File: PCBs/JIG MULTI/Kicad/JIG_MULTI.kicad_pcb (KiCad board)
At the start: 2 copper layers, 85.1 x 73.7 mm, 19 parts, among them U0 12pad, U1 12pad

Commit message: Fixed resistor value for 5V circuit
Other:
- board text added: "R1 = 2K R2 = 1K R3 = 1K R4 = 150 R5 = 2K R6 = 7.5K"
- board text removed: "R1 = 1K R2 = 1K R3 = 1K R4 = 150 R5 = 2K R6 = 7.5K"
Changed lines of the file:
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@@
     (effects (font (size 2 2) (thickness 0.4) bold) (justify left bottom))
   )
-  (gr_text "R1 = 1K\nR2 = 1K\nR3 = 1K\nR4 = 150\nR5 = 2K\nR6 = 7.5K" (at 43.18 96.52) (layer "F.SilkS")
+  (gr_text "R1 = 2K\nR2 = 1K\nR3 = 1K\nR4 = 150\nR5 = 2K\nR6 = 7.5K" (at 43.18 96.52) (layer "F.SilkS")
     (effects (font (size 2 2) (thickness 0.1)) (justify left bottom))
   )

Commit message: Added a warning label at the back of the board
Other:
- board text added: "** CAUTION ** Some UART modules advertised as 5V or with a jumper to 5V do NOT shift the power levels for UART TX/RX which will operate at 3.3V, Please measure voltage on your UART module between TX and GND. if it runs at 3.3V Replace R5 to a 1K ohms resistor."
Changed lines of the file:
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@@
   (gr_line (start 58.42 93.98) (end 58.42 99.06)
     (stroke (width 0.25) (type default)) (layer "F.Cu"))
+  (gr_rect (start 33.5 43.18) (end 114.78 55.88)
+    (stroke (width 0.2) (type default)) (fill none) (layer "B.SilkS"))
   (gr_rect (start 106.68 91.02) (end 111.76 96.52)
     (stroke (width 0.2) (type default)) (fill none) (layer "F.SilkS"))
@@
     (effects (font (size 2 2) (thickness 0.4) bold) (justify left bottom mirror))
   )
+  (gr_text "** CAUTION ** \n\n\nSome UART modules advertised as 5V or with a jumper to 5V do NOT shift the power levels for UART TX/RX \nwhich will operate at 3.3V, Please measure voltage on your UART module between TX and GND.\nif it runs at 3.3V Replace R5 to a 1K ohms resistor." (at 114.3 53.34) (layer "B.SilkS")
+    (effects (font (size 1 1) (thickness 0.2) bold) (justify left bottom mirror))
+  )
   (gr_text "PCH-1K Only" (at 105 80.5 90) (layer "F.SilkS")

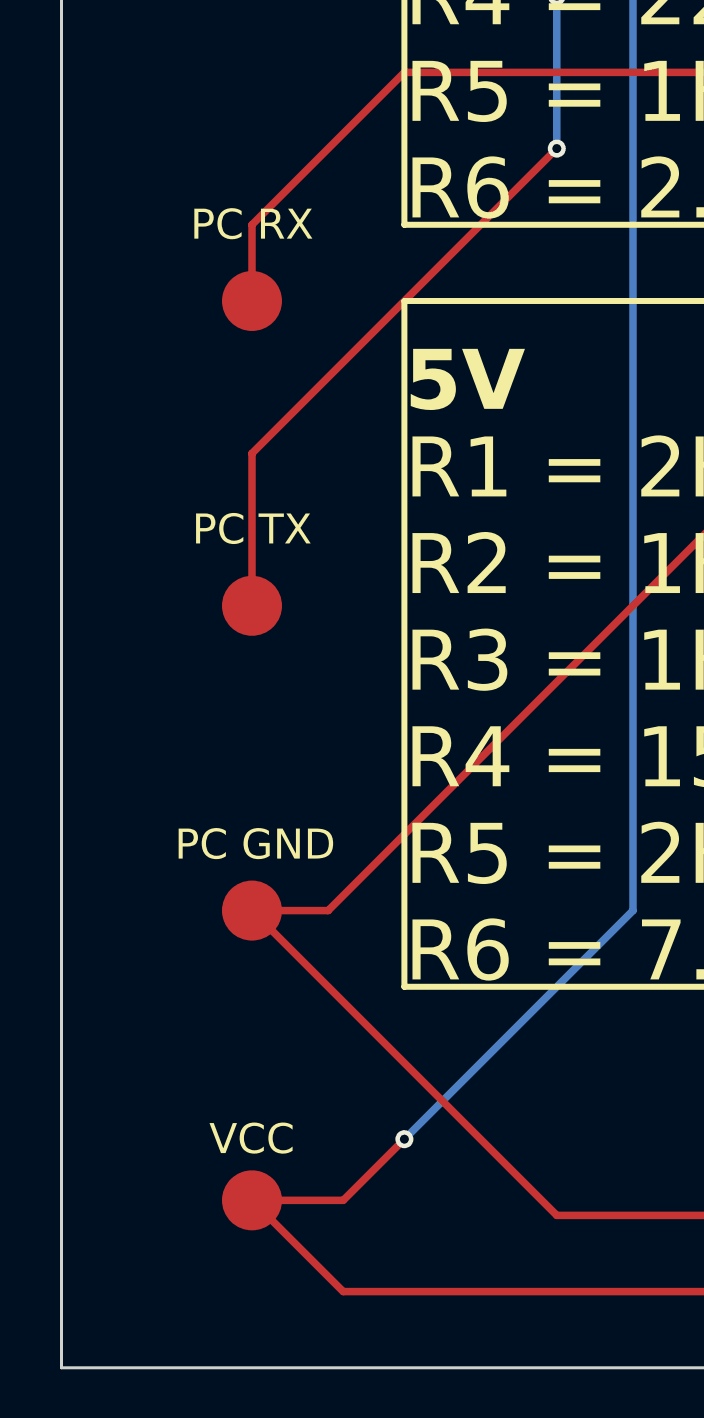
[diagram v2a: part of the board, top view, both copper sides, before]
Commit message: Used proper footprints for some of the pads that were missing them.
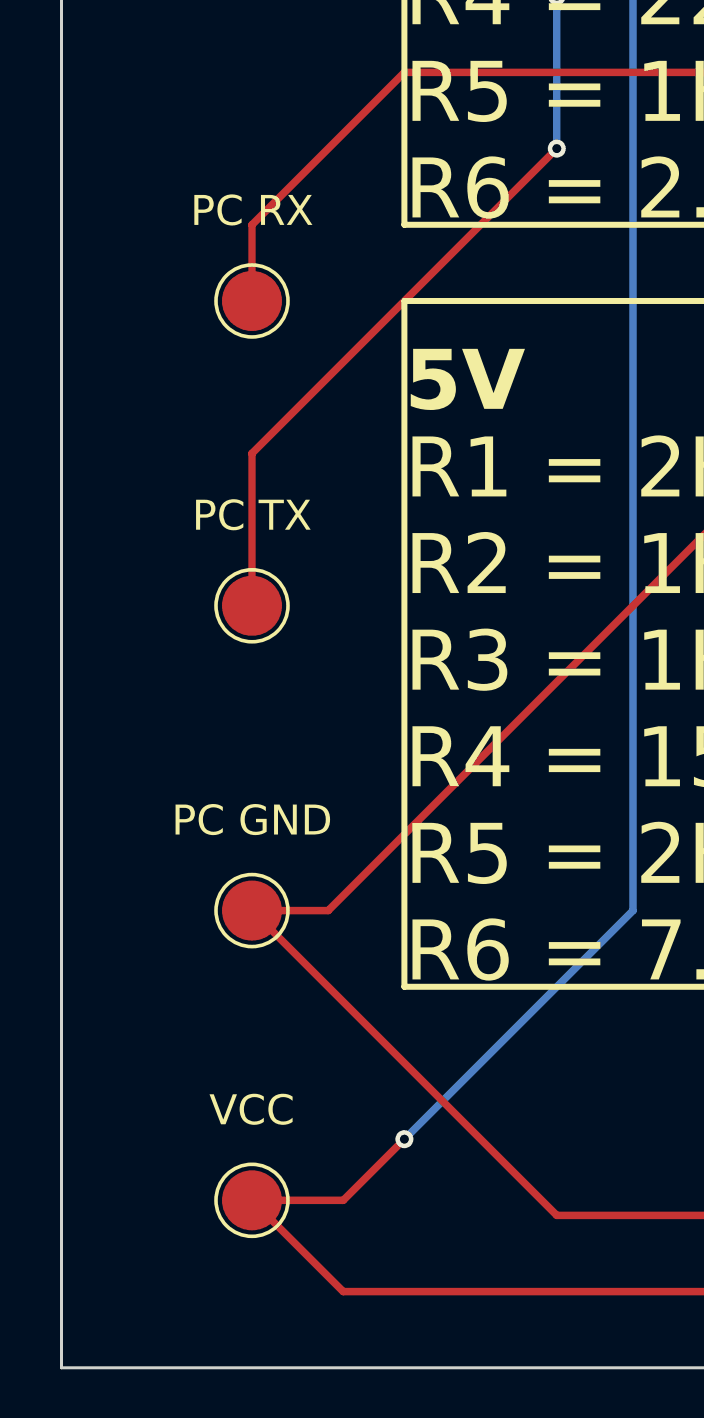
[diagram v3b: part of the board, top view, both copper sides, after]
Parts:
- removed ? (x4): , 
- added PC GND: TestPoint_Pad_D2.0mm, TestPoint:TestPoint_Pad_D2.0mm, F.Cu at (38.1, 94.0)
- added PC RX: TestPoint_Pad_D2.0mm, TestPoint:TestPoint_Pad_D2.0mm, F.Cu at (38.1, 73.7)
- added PC TX: TestPoint_Pad_D2.0mm, TestPoint:TestPoint_Pad_D2.0mm, F.Cu at (38.1, 83.8)
- added VCC: TestPoint_Pad_D2.0mm, TestPoint:TestPoint_Pad_D2.0mm, F.Cu at (38.1, 103.6)
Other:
- board text removed: "PC GND"
- board text removed: "PC RX"
- board text removed: "PC TX"
- board text removed: "VCC"
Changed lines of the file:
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@@
     (pad "12" thru_hole circle (at 27.94 0) (size 1.524 1.524) (drill 0.914) (layers "*.Cu" "*.Paste" "*.Mask"))
+  )
+  (footprint "TestPoint:TestPoint_Pad_D2.0mm" (layer "F.Cu")
+    (at 38.1 83.82)
+    (descr "SMD pad as test Point, diameter 2.0mm")
+    (tags "test point SMD pad")
+    (attr exclude_from_pos_files exclude_from_bom)
+    (fp_text reference "PC TX" (at 0 -2.998) (layer "F.SilkS")
+        (effects (font (size 1 1) (thickness 0.15)))
+    )
+    (fp_text value "TestPoint_Pad_D2.0mm" (at 0 2.05) (layer "F.Fab")
+        (effects (font (size 1 1) (thickness 0.15)))
+    )
+    (fp_text user "${REFERENCE}" (at 0 -2) (layer "F.Fab")
+        (effects (font (size 1 1) (thickness 0.15)))
+    )
+    (fp_circle (center 0 0) (end 0 1.2)
+      (stroke (width 0.12) (type solid)) (fill none) (layer "F.SilkS"))
+    (fp_circle (center 0 0) (end 1.5 0)
+      (stroke (width 0.05) (type solid)) (fill none) (layer "F.CrtYd"))
+    (pad "2" smd circle (at 0 0) (size 2 2) (layers "F.Cu" "F.Mask"))
   )
   (footprint "Resistor_THT:R_Axial_DIN0309_L9.0mm_D3.2mm_P12.70mm_Horizontal" (layer "F.Cu")
@@
     (pad "8" smd circle (at 0 0) (size 2 2) (layers "F.Cu" "F.Mask"))
   )
-  (footprint "" (layer "F.Cu")
-    (at 38.1 103.637944)
-    (fp_text reference "" (at 0 0) (layer "F.SilkS")
-        (effects (font (size 1.27 1.27) (thickness 0.15)))
-    )
-    (fp_text value "" (at 0 0) (layer "F.SilkS")
-        (effects (font (size 1.27 1.27) (thickness 0.15)))
-    )
-    (pad "4" smd circle (at 0 0) (size 2 2) (layers "F.Cu" "F.Mask"))
-  )
   (footprint "Resistor_THT:R_Axial_DIN0309_L9.0mm_D3.2mm_P12.70mm_Horizontal" (layer "F.Cu")
     (at 58.42 99.06)
@@
       (stroke (width 0.05) (type solid)) (fill none) (layer "F.CrtYd"))
     (pad "6" smd circle (at 0 0) (size 2 2) (layers "F.Cu" "F.Mask"))
+  )
+  (footprint "TestPoint:TestPoint_Pad_D2.0mm" (layer "F.Cu")
+    (at 38.1 103.637944)
+    (descr "SMD pad as test Point, diameter 2.0mm")
+    (tags "test point SMD pad")
+    (attr exclude_from_pos_files exclude_from_bom)
+    (fp_text reference "VCC" (at 0 -2.998) (layer "F.SilkS")
+        (effects (font (size 1 1) (thickness 0.15)))
+    )
+    (fp_text value "TestPoint_Pad_D2.0mm" (at 0 2.05) (layer "F.Fab")
+        (effects (font (size 1 1) (thickness 0.15)))
+    )
+    (fp_text user "${REFERENCE}" (at 0 -2) (layer "F.Fab")
+        (effects (font (size 1 1) (thickness 0.15)))
+    )
+    (fp_circle (center 0 0) (end 0 1.2)
+      (stroke (width 0.12) (type solid)) (fill none) (layer "F.SilkS"))
+    (fp_circle (center 0 0) (end 1.5 0)
+      (stroke (width 0.05) (type solid)) (fill none) (layer "F.CrtYd"))
+    (pad "4" smd circle (at 0 0) (size 2 2) (layers "F.Cu" "F.Mask"))
+  )
+  (footprint "TestPoint:TestPoint_Pad_D2.0mm" (layer "F.Cu")
+    (at 38.1 73.66)
+    (descr "SMD pad as test Point, diameter 2.0mm")
+    (tags "test point SMD pad")
+    (attr exclude_from_pos_files exclude_from_bom)
+    (fp_text reference "PC RX" (at 0 -2.998) (layer "F.SilkS")
+        (effects (font (size 1 1) (thickness 0.15)))
+    )
+    (fp_text value "TestPoint_Pad_D2.0mm" (at 0 2.05) (layer "F.Fab")
+        (effects (font (size 1 1) (thickness 0.15)))
+    )
+    (fp_text user "${REFERENCE}" (at 0 -2) (layer "F.Fab")
+        (effects (font (size 1 1) (thickness 0.15)))
+    )
+    (fp_circle (center 0 0) (end 0 1.2)
+      (stroke (width 0.12) (type solid)) (fill none) (layer "F.SilkS"))
+    (fp_circle (center 0 0) (end 1.5 0)
+      (stroke (width 0.05) (type solid)) (fill none) (layer "F.CrtYd"))
+    (pad "1" smd circle (at 0 0) (size 2 2) (layers "F.Cu" "F.Mask"))
   )
   (footprint "Resistor_THT:R_Axial_DIN0309_L9.0mm_D3.2mm_P12.70mm_Horizontal" (layer "F.Cu")
@@
     (pad "29" thru_hole oval (at 11.5 1.5) (size 1 2) (drill oval 0.75 1.75) (layers "*.Cu" "*.Paste" "*.Mask"))
   )
-  (footprint "" (layer "F.Cu")
-    (at 38.1 73.66)
-    (fp_text reference "" (at 0 0) (layer "F.SilkS")
-        (effects (font (size 1.27 1.27) (thickness 0.15)))
-    )
-    (fp_text value "" (at 0 0) (layer "F.SilkS")
-        (effects (font (size 1.27 1.27) (thickness 0.15)))
-    )
-    (pad "1" smd circle (at 0 0) (size 2 2) (layers "F.Cu" "F.Mask"))
-  )
-  (footprint "" (layer "F.Cu")
+  (footprint "TestPoint:TestPoint_Pad_D2.0mm" (layer "F.Cu")
     (at 38.1 93.98)
-    (fp_text reference "" (at 0 0) (layer "F.SilkS")
-        (effects (font (size 1.27 1.27) (thickness 0.15)))
-    )
-    (fp_text value "" (at 0 0) (layer "F.SilkS")
-        (effects (font (size 1.27 1.27) (thickness 0.15)))
-    )
+    (descr "SMD pad as test Point, diameter 2.0mm")
+    (tags "test point SMD pad")
+    (attr exclude_from_pos_files exclude_from_bom)
+    (fp_text reference "PC GND" (at 0 -2.998) (layer "F.SilkS")
+        (effects (font (size 1 1) (thickness 0.15)))
+    )
+    (fp_text value "TestPoint_Pad_D2.0mm" (at 0 2.05) (layer "F.Fab")
+        (effects (font (size 1 1) (thickness 0.15)))
+    )
+    (fp_text user "${REFERENCE}" (at 0 -2) (layer "F.Fab")
+        (effects (font (size 1 1) (thickness 0.15)))
+    )
+    (fp_circle (center 0 0) (end 0 1.2)
+      (stroke (width 0.12) (type solid)) (fill none) (layer "F.SilkS"))
+    (fp_circle (center 0 0) (end 1.5 0)
+      (stroke (width 0.05) (type solid)) (fill none) (layer "F.CrtYd"))
     (pad "3" smd circle (at 0 0) (size 2 2) (layers "F.Cu" "F.Mask"))
   )
@@
       (rotate (xyz 0 0 0))
     )
-  )
-  (footprint "" (layer "F.Cu")
-    (at 38.1 83.82)
-    (fp_text reference "" (at 0 0) (layer "F.SilkS")
-        (effects (font (size 1.27 1.27) (thickness 0.15)))
-    )
-    (fp_text value "" (at 0 0) (layer "F.SilkS")
-        (effects (font (size 1.27 1.27) (thickness 0.15)))
-    )
-    (pad "2" smd circle (at 0 0) (size 2 2) (layers "F.Cu" "F.Mask"))
   )
   (gr_line (start 109.22 93.98) (end 58.42 93.98)
@@
     (effects (font (size 1 1) (thickness 0.2)) (justify left bottom))
   )
-  (gr_text "PC GND" (at 38.202681 91.783349) (layer "F.SilkS")
-    (effects (font (size 1 1) (thickness 0.15)))
-  )
   (gr_text "UDC 11 = JIG SENSE 1\nUDC 12 = JIG SENSE 2" (at 63.5 58.42) (layer "F.SilkS")
     (effects (font (size 2 2) (thickness 0.1)) (justify left bottom))
@@
     (effects (font (size 2 2) (thickness 0.1)) (justify left bottom))
   )
-  (gr_text "PC RX" (at 38.1 71.12) (layer "F.SilkS")
-    (effects (font (size 1 1) (thickness 0.15)))
-  )
   (gr_text "GND" (at 109.22 86.36) (layer "F.SilkS")
     (effects (font (size 1 1) (thickness 0.15)))
@@
     (effects (font (size 2 2) (thickness 0.1)) (justify left bottom))
   )
-  (gr_text "PC TX" (at 38.1 81.28) (layer "F.SilkS")
-    (effects (font (size 1 1) (thickness 0.15)))
-  )
   (gr_text "3.3V" (at 43.18 52) (layer "F.SilkS")
     (effects (font (size 2 2) (thickness 0.4) bold) (justify left bottom))
   )
-  (gr_text "VCC" (at 38.1 101.6) (layer "F.SilkS")
-    (effects (font (size 1 1) (thickness 0.15)))
-  )
   (gr_text "PCH JIG MULTI BOARD 2.0\nBy Mathieulh" (at 83.82 43.18) (layer "F.SilkS")
